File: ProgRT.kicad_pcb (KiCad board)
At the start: 2 copper layers, 99.7 x 49.5 mm, 66 parts

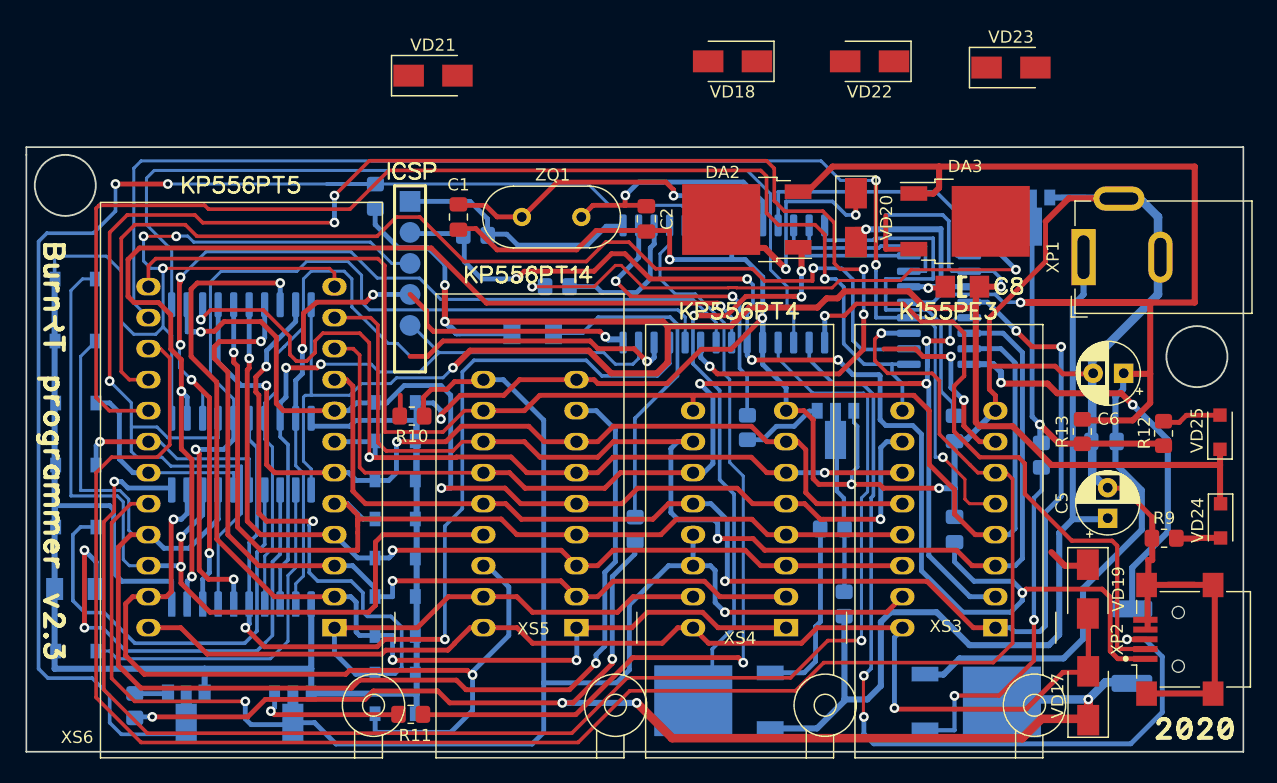
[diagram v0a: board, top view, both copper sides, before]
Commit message: Routing complete
All the parts placed and connected
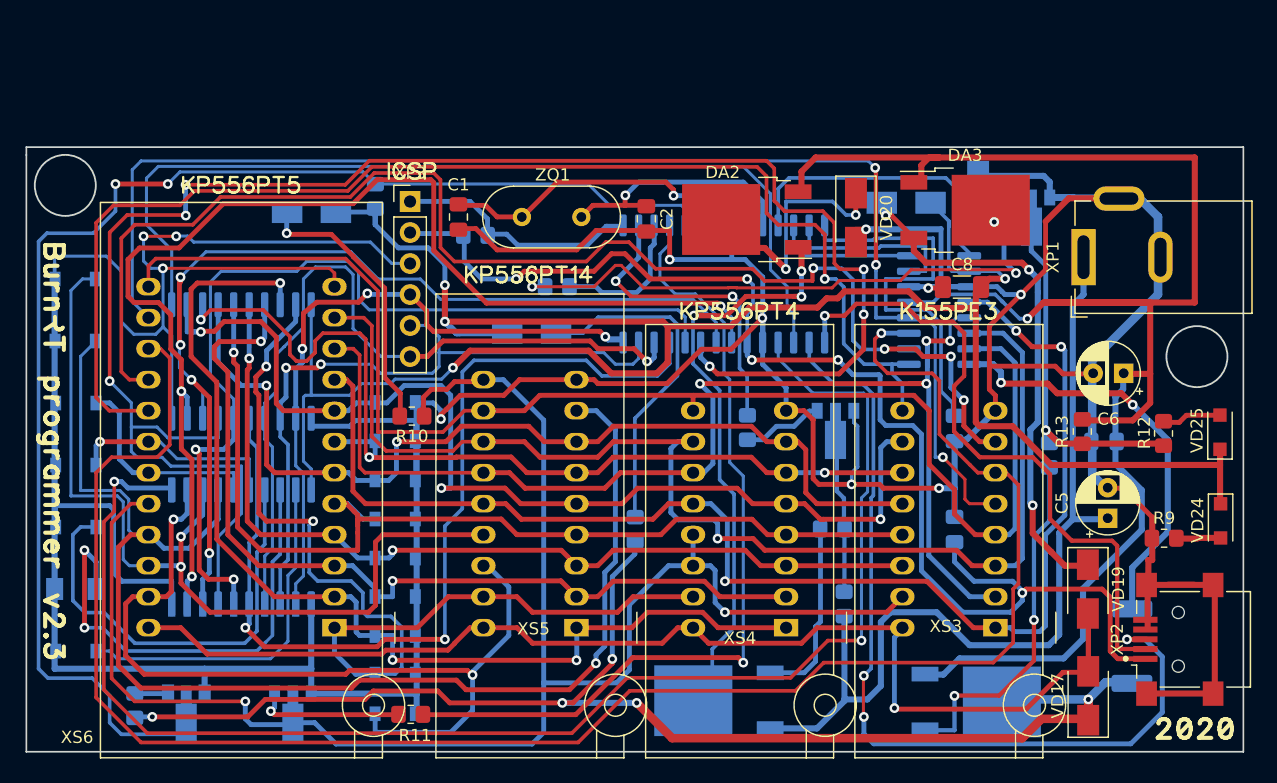
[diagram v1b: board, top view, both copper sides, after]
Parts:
- added C8: 100n, Capacitor_SMD:C_1206_3216Metric_Pad1.33x1.80mm_HandSolder, F.Cu at (165.3, 75.2)
- added XP3: Conn_01x06, Connector_PinHeader_2.54mm:PinHeader_1x06_P2.54mm_Vertical, F.Cu at (120.0, 68.2)
- VD18, VD21, VD22, VD23: moved to B.Cu
- moved VD18 27.7 mm to (130.0, 79.0), turned to 0 degrees
- moved VD21 15.0 mm to (112.0, 69.1), turned to 180 degrees
- moved VD22 12.0 mm to (160.7, 68.3), turned to 0 degrees
- moved VD23 11.2 mm to (166.6, 68.1), turned to 90 degrees
- moved DA3 0.91 mm to (165.5, 68.9)
- moved R14 0.66 mm to (172.4, 89.0)
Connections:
- net Net-(DD1-Pad1) renamed /MCLR
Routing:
- net Net-(DA3-Pad3): track 8.24 -> 43.3 mm, vias 0 -> 3
- net Net-(R10-Pad2): track 1.75 -> 22.7 mm, vias 0 -> 1
- net /GND: track 519.7 -> 531.9 mm, vias 10 -> 11
- net /D0: track 88.4 -> 96.3 mm
- net /IO6: track 106.2 -> 111.7 mm, vias 3 -> 4
- net /~{RD}: track 114.5 -> 111.3 mm
- net Net-(R12-Pad2): track 31.6 -> 29.3 mm
- net /D6: track 55.6 -> 57.2 mm
- net /D5: track 64.6 -> 66.2 mm
- net /B0: track 22.8 -> 24.3 mm
- net Net-(DA3-Pad2): track 0.00 -> 1.41 mm, vias 0 -> 1
- net /IO3: track 115.6 -> 114.4 mm
- net /IO7: track 105.5 -> 104.8 mm
- net /D-: track 52.6 -> 53.3 mm
- net /IO4: track 109.4 -> 110.1 mm
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
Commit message: Fix DRC errors
DRC now (almost) passes. Only ZIF socket courtyard overlaps remain, i can't do
anything about them, at least for now
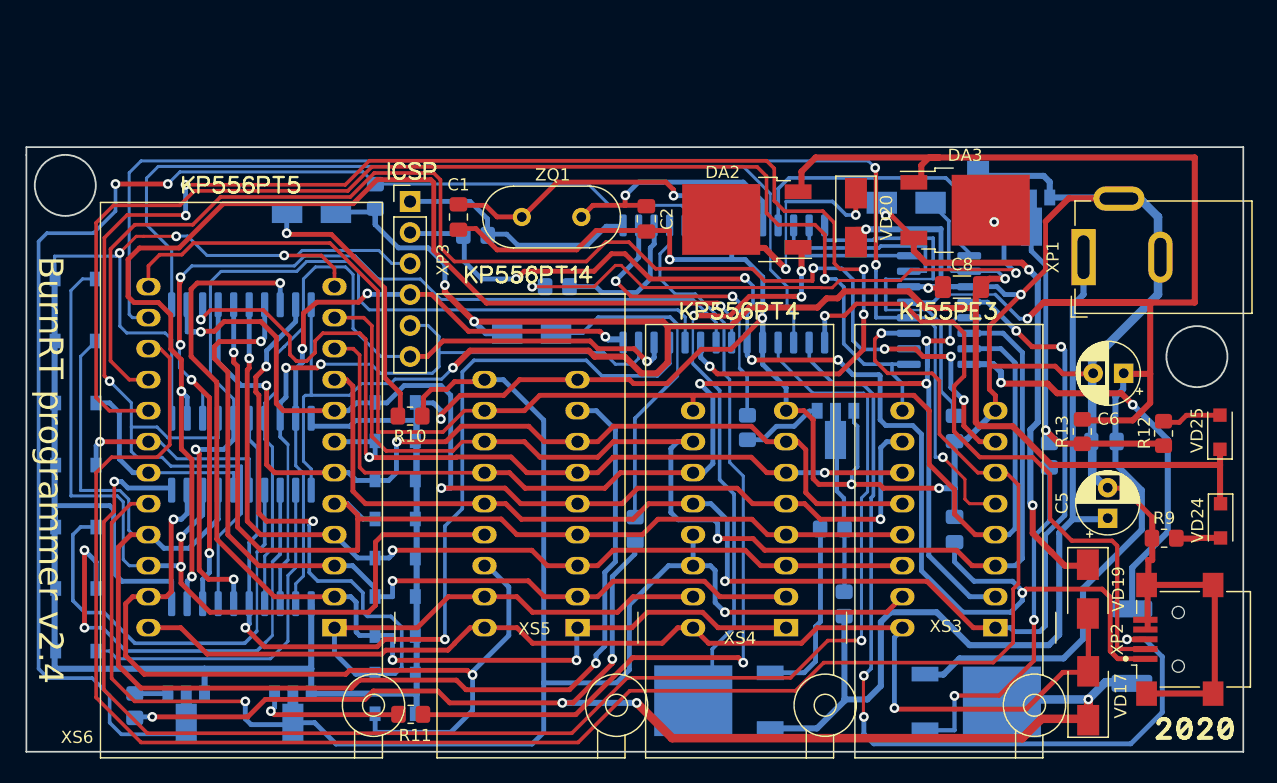
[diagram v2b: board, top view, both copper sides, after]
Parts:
- moved R10 0.15 mm to (120.0, 85.8)
- moved XS5 0.09 mm to (133.8, 103.1)
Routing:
- net /GND: track 531.9 -> 497.8 mm
- net /+5V: track 171.8 -> 165.9 mm
- net Net-(DA2-Pad2): track 21.6 -> 19.3 mm
- net Net-(DA2-Pad1): track 51.5 -> 49.6 mm
- net /~{CS}: track 138.3 -> 136.7 mm
- net /~{RD}: track 111.3 -> 109.8 mm
- net /IO3: track 114.4 -> 115.5 mm
- net /IO4: track 110.1 -> 111.1 mm
- net /IO5: track 151.6 -> 150.7 mm
- net Net-(R12-Pad2): track 29.3 -> 28.6 mm
- net /D7: track 53.6 -> 53.0 mm
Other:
- board text added: "BurnRT programmer v2.4"

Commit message: Add mounting holes
Replace drawing with proper mounting hole definitions
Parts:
- added REF**: MountingHole_2.5mm, MountingHole:MountingHole_2.5mm, F.Cu at (91.8, 110.2)
- added REF**: MountingHole_2.5mm, MountingHole:MountingHole_2.5mm, F.Cu at (184.5, 81.0)
- added REF**: MountingHole_2.5mm, MountingHole:MountingHole_2.5mm, F.Cu at (91.8, 66.9)
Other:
- outline, holes or cut-outs redrawn

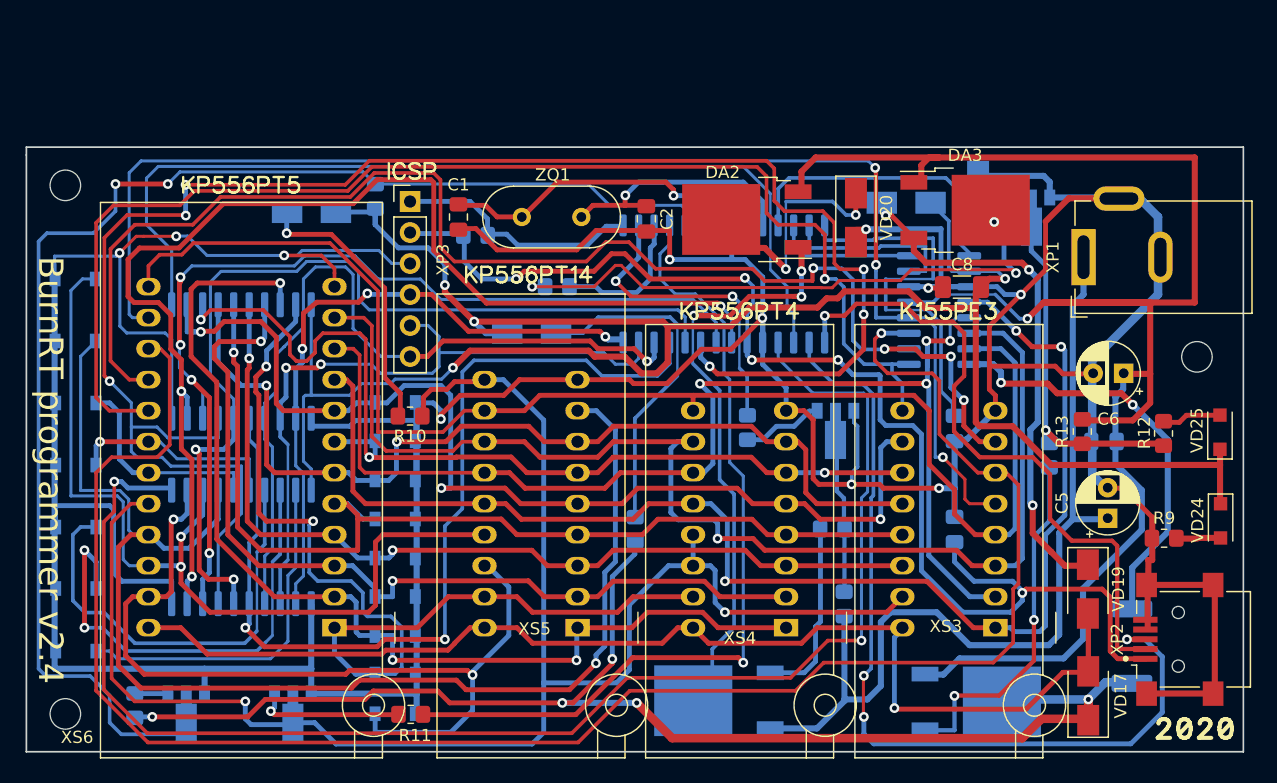
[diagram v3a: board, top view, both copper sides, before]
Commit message: Some PCB optimizations
Removed some vias, rerouted some tracks, added ground plane
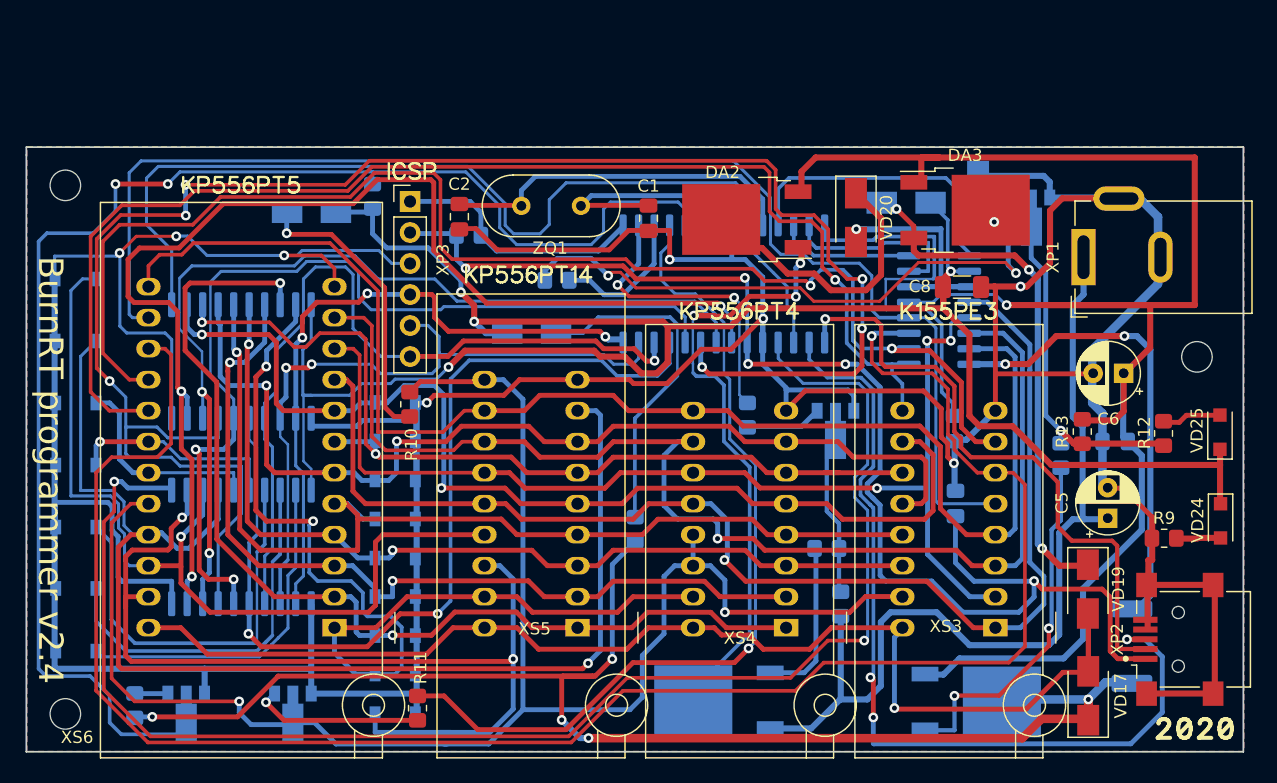
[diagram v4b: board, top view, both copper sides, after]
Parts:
- moved C1 15.6 mm to (139.6, 69.6)
- moved C2 15.3 mm to (124.1, 69.5)
- moved ZQ1 5.00 mm to (129.2, 68.6), turned to 0 degrees
- moved C4 2.13 mm to (164.7, 93.0)
- moved R3 1.66 mm to (154.2, 96.6)
- moved R4 1.02 mm to (147.7, 85.7)
- moved R10 0.97 mm to (120.0, 84.8), turned to -90 degrees
- moved R14 0.94 mm to (173.4, 89.0)
- moved C7 0.91 mm to (177.8, 87.9)
- moved R11 0.76 mm to (120.7, 109.7), turned to -90 degrees
- moved R1 0.56 mm to (124.8, 71.0)
- moved R15 0.52 mm to (132.1, 74.7)
- moved R2 0.28 mm to (155.3, 101.2)
- moved R6 0.23 mm to (117.0, 67.8)
- turned C8 to 180 degrees
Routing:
- net /GND: track 497.8 -> 483.0 mm, vias 11 -> 9
- net /A8: track 71.2 -> 80.3 mm
- net /IO1: track 100.7 -> 91.6 mm, vias 4 -> 3
- net /CLKO: track 20.8 -> 29.5 mm, vias 1 -> 0
- net /A14: track 38.8 -> 30.9 mm, vias 2 -> 0
- net /~{RD}: track 109.8 -> 117.0 mm
- net /CLKI: track 28.0 -> 21.4 mm, vias 1 -> 0
- net /+5V: track 165.9 -> 160.7 mm
- net /IO0: track 108.7 -> 103.6 mm, vias 3 -> 1
- net /L0: track 76.3 -> 81.1 mm
- net /+12V: track 139.5 -> 135.0 mm
- net /UPR: track 112.0 -> 116.4 mm
- net /A2: track 77.7 -> 81.9 mm
- net Net-(DA1-Pad8): track 34.5 -> 38.3 mm
- net /A10: track 108.5 -> 104.8 mm
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- added copper zone on B.Cu, net /GND
- added copper zone on F.Cu, net /GND

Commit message: Small footprint corrections
- use SMF footprint for Zener diodes, easier to hand-solder
- use larger footprint for polar caps, extends availability
- use 3216 LEDs, easier available and easier to hand-solder
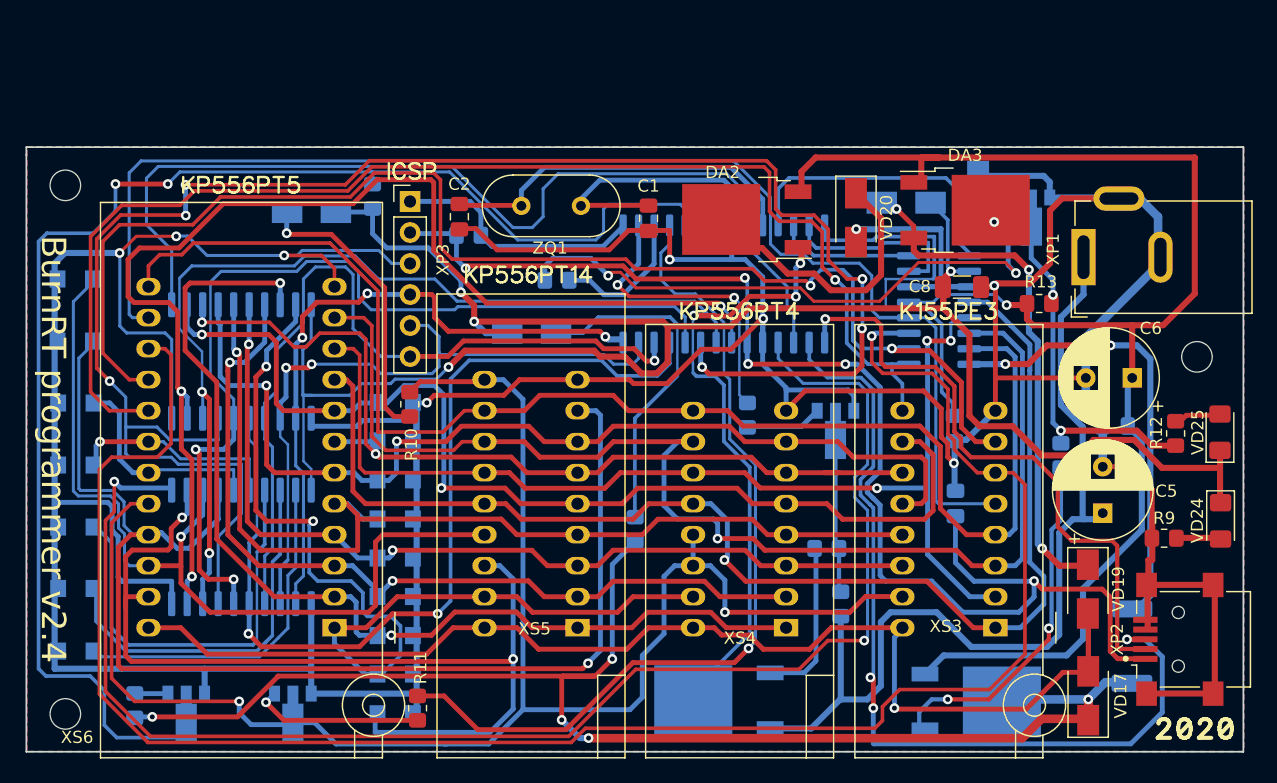
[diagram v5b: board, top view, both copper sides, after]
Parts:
- C5, C6: footprint Capacitor_THT:CP_Radial_D5.0mm_P2.50mm -> Capacitor_THT:CP_Radial_D8.0mm_P3.80mm
- VD1, VD10, VD11, VD12, VD13, VD14, VD15, VD16, VD2, VD3, VD4, VD5, VD6, VD7, VD8, VD9: footprint Diode_SMD:D_SOD-123 -> Diode_SMD:D_SMF
- VD24, VD25: footprint Diode_SMD:D_SOD-123F -> LED_SMD:LED_1206_3216Metric_Pad1.42x1.75mm_HandSolder
- moved R13 11.1 mm to (171.6, 76.6), turned to 180 degrees
- moved C7 1.27 mm to (177.8, 86.6)
- moved R12 0.99 mm to (182.8, 87.2)
- moved C6 0.80 mm to (179.2, 82.7)
- moved C5 0.58 mm to (176.8, 93.8)
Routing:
- net /+12V: track 135.0 -> 118.4 mm
- net /GND: track 483.0 -> 473.5 mm
- net Net-(R12-Pad2): track 28.2 -> 30.0 mm, vias 1 -> 2
- net /CLKI: track 21.4 -> 22.7 mm
- net /A9: track 72.9 -> 71.7 mm
- net /A7: track 81.3 -> 80.1 mm
- net /+5V: track 160.7 -> 161.9 mm
- net Net-(DA1-Pad8): track 38.3 -> 37.2 mm
- net Net-(R14-Pad2): track 30.1 -> 29.1 mm
- net Net-(R12-Pad1): track 4.85 -> 3.84 mm
- net /~{RD}: track 117.0 -> 116.1 mm
- net /A8: track 80.3 -> 79.4 mm
- net /IO5: track 153.0 -> 153.8 mm
- net /A5: track 71.9 -> 71.2 mm
- net /L0: track 81.1 -> 80.4 mm
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
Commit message: Use MiniMELF Zeners
Change Zener diodes package again to MiniMELF. Should be easier to hand-solder.
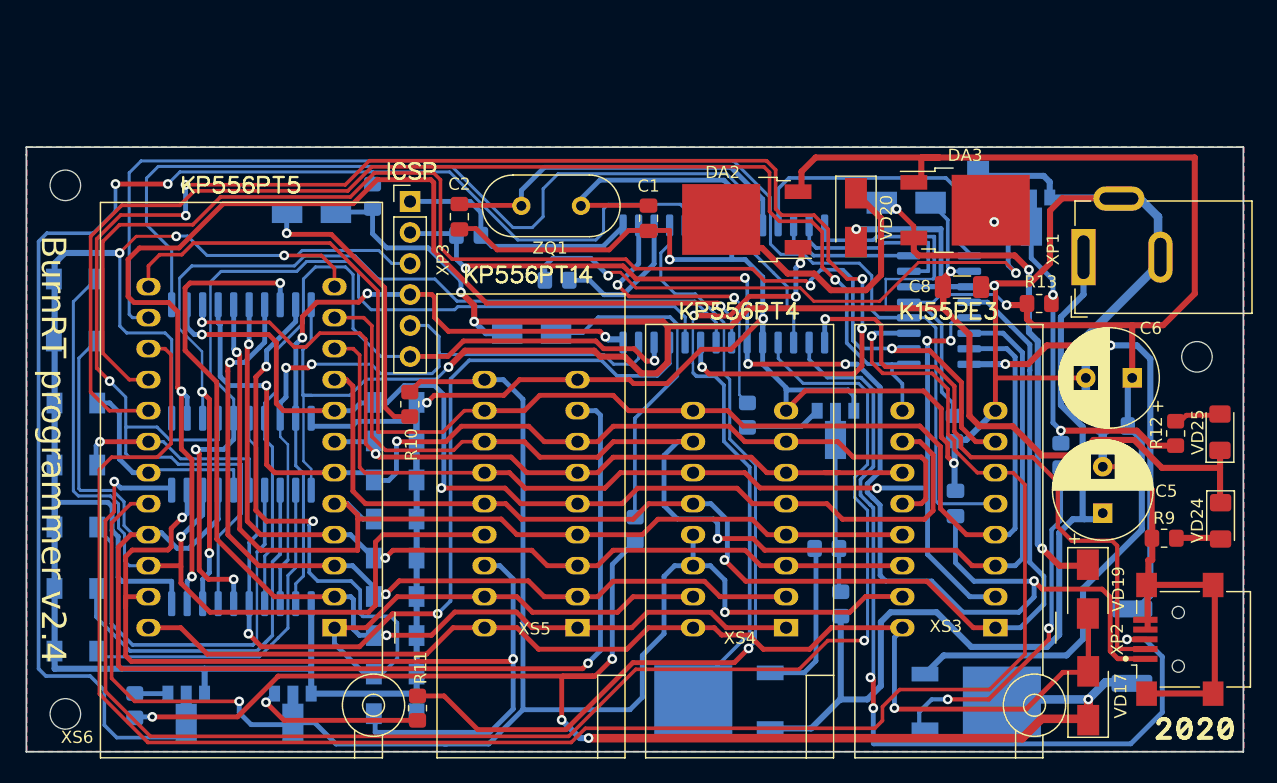
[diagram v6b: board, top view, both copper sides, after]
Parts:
- VD1, VD10, VD11, VD12, VD13, VD14, VD15, VD16, VD2, VD3, VD4, VD5, VD6, VD7, VD8, VD9: footprint Diode_SMD:D_SMF -> Diode_SMD:D_MiniMELF

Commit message: Fix diodes on silk screen
Diodes were reversed because pin numbers got corrupted during import. Fix them,
so that silk screen and fab layer is displayed correctly
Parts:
- turned VD1 to 0 degrees
- turned VD10 to 180 degrees
- turned VD11 to 180 degrees
- turned VD12 to 180 degrees
- turned VD13 to 180 degrees
- turned VD14 to 180 degrees
- turned VD15 to 180 degrees
- turned VD16 to 0 degrees
- turned VD17 to -90 degrees
- turned VD18 to 180 degrees
- turned VD19 to 90 degrees
- turned VD2 to 0 degrees
- turned VD20 to 90 degrees
- turned VD21 to 0 degrees
- turned VD22 to 180 degrees
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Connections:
- VD1 pad 1: /GND -> /A7
- VD1 pad 2: /A7 -> /GND
- VD10 pad 1: /GND -> /A14
- VD10 pad 2: /A14 -> /GND
- VD11 pad 1: /GND -> /A13
- VD11 pad 2: /A13 -> /GND
- VD12 pad 1: /GND -> /A12
- VD12 pad 2: /A12 -> /GND
- VD13 pad 1: /GND -> /A11
- VD13 pad 2: /A11 -> /GND
- VD14 pad 1: /GND -> /A10
- VD14 pad 2: /A10 -> /GND
- VD15 pad 1: /GND -> /A9
- VD15 pad 2: /A9 -> /GND
- VD16 pad 1: /GND -> /A8
- VD16 pad 2: /A8 -> /GND
- VD17 pad 1: /UPR -> /VCC
- VD17 pad 2: /VCC -> /UPR
- VD18 pad 1: /+5V -> Net-(R5-Pad2)
- VD18 pad 2: Net-(R5-Pad2) -> /+5V
- VD19 pad 1: Net-(DA3-Pad3) -> /VCC
- VD19 pad 2: /VCC -> Net-(DA3-Pad3)
- VD2 pad 1: /GND -> /A6
- VD2 pad 2: /A6 -> /GND
- VD20 pad 1: Net-(DA2-Pad2) -> /GND
- VD20 pad 2: /GND -> Net-(DA2-Pad2)
- VD21 pad 1: /+5V -> Net-(R10-Pad2)
- VD21 pad 2: Net-(R10-Pad2) -> /+5V
- VD22 pad 1: Net-(DA3-Pad3) -> /+5V
- VD22 pad 2: /+5V -> Net-(DA3-Pad3)
- VD23 pad 1: Net-(DA3-Pad2) -> /GND
- VD23 pad 2: /GND -> Net-(DA3-Pad2)
- VD24 pad 1: /+5V -> Net-(R9-Pad2)
- VD24 pad 2: Net-(R9-Pad2) -> /+5V
- VD25 pad 1: /+5V -> Net-(R12-Pad1)
- VD25 pad 2: Net-(R12-Pad1) -> /+5V
- VD3 pad 1: /GND -> /A5
- VD3 pad 2: /A5 -> /GND
- VD4 pad 1: /GND -> /A4
- VD4 pad 2: /A4 -> /GND
- VD5 pad 1: /GND -> /A3
- VD5 pad 2: /A3 -> /GND
- VD6 pad 1: /GND -> /A2
- VD6 pad 2: /A2 -> /GND
- VD7 pad 1: /GND -> /A1
- VD7 pad 2: /A1 -> /GND
- VD8 pad 1: /GND -> /A0
- VD8 pad 2: /A0 -> /GND
- VD9 pad 1: /GND -> /A15
- VD9 pad 2: /A15 -> /GND
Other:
- board text added: "2022"
